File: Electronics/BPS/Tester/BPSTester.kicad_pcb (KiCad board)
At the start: 2 copper layers, 26 parts, among them J1 Conn_01x13_Male

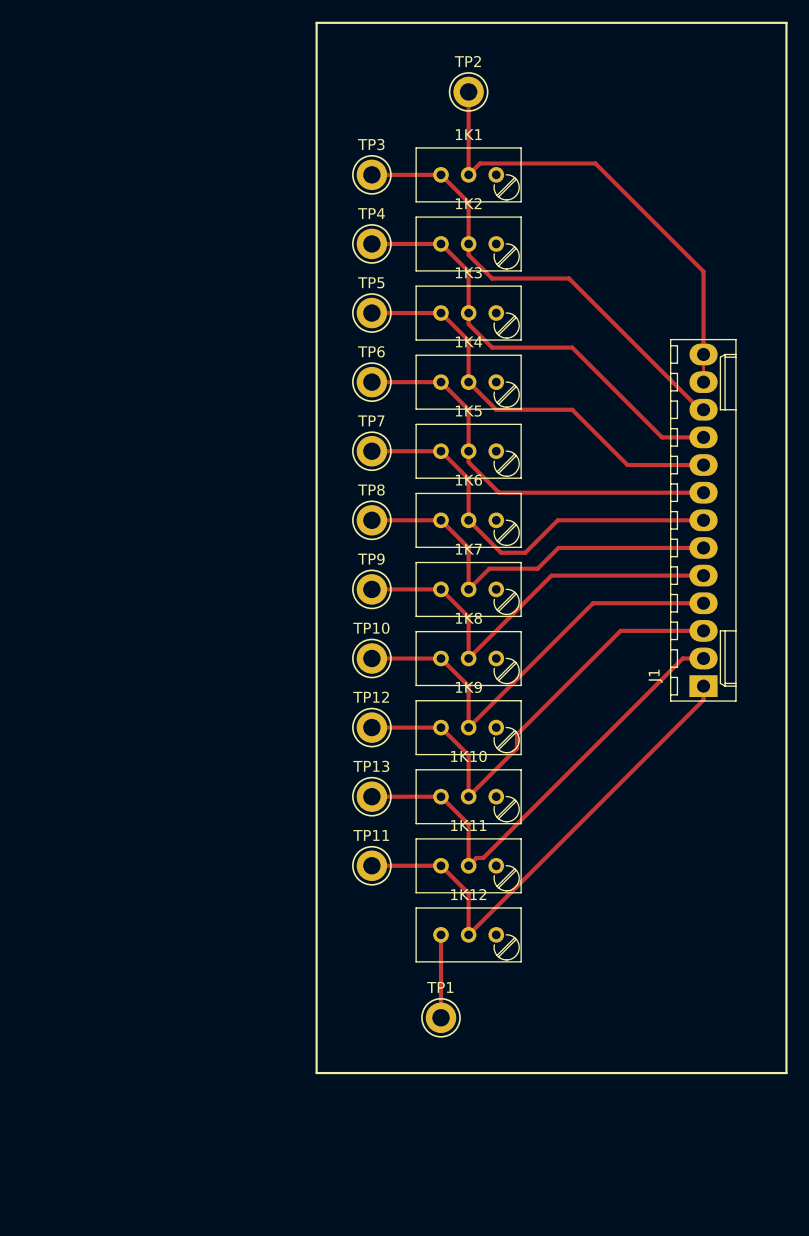
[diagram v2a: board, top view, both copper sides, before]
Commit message: Placed a ground plane and labeled Testing board
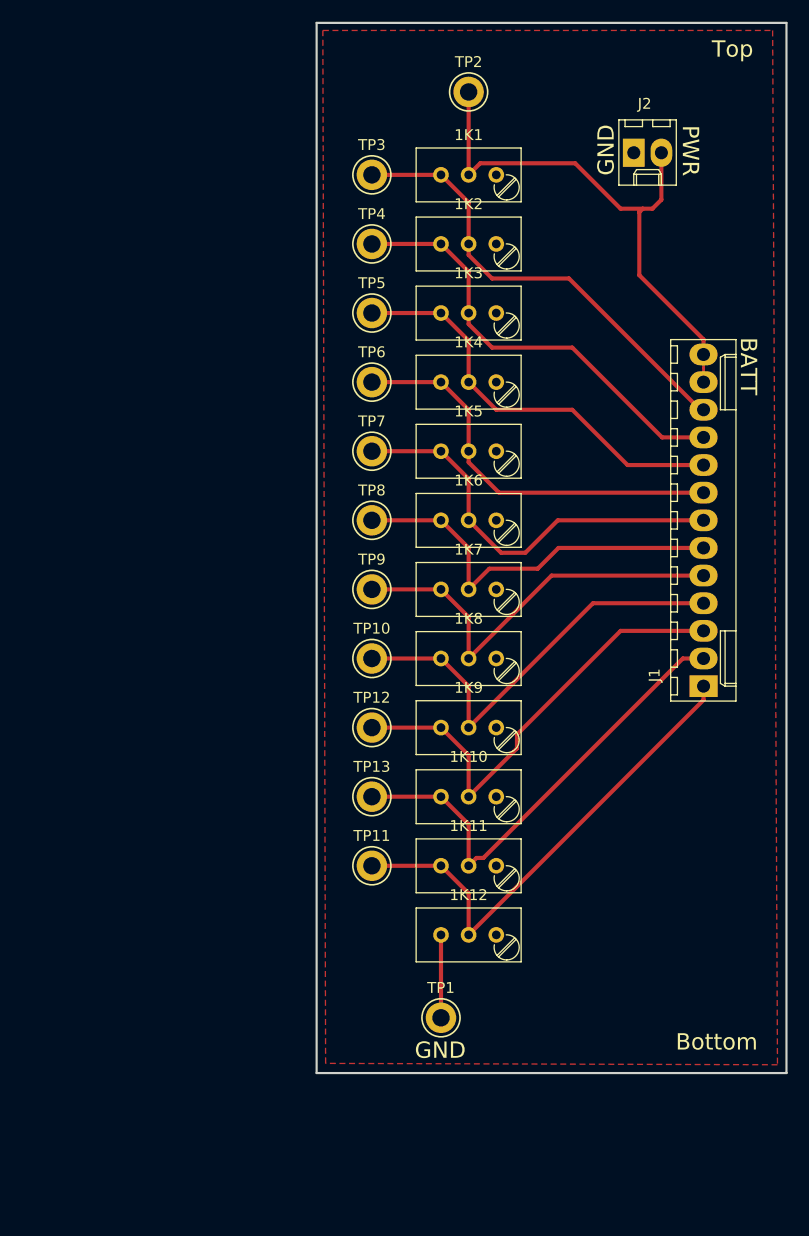
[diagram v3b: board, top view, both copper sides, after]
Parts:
- added J2: Conn_01x02_Male, Connectors_Molex:Molex_KK-6410-02_02x2.54mm_Straight, F.Cu at (156.1, 52.6)
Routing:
- net +BATT: track 43.9 -> 50.7 mm
- net GND: track 7.62 -> 8.19 mm
- added copper zone on F.Cu, net GND
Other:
- board outline added: 43.2 x 96.5 mm
- board text added: "BATT"
- board text added: "Bottom"
- board text added: "GND"
- board text added: "PWR"
- board text added: "Top"
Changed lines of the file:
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@@
   (general
     (thickness 1.6)
-    (drawings 4)
-    (tracks 80)
+    (drawings 10)
+    (tracks 90)
     (zones 0)
-    (modules 26)
+    (modules 27)
     (nets 26)
   )
@@
     (trace_min 0.2)
     (segment_width 0.2)
-    (edge_width 0.15)
+    (edge_width 0.2)
     (via_size 0.762)
     (via_drill 0.381)
@@
     (add_net "Net-(1K8-Pad3)")
     (add_net "Net-(1K9-Pad1)")
+  )
+  (module Connectors_Molex:Molex_KK-6410-02_02x2.54mm_Straight (layer F.Cu)
+    (at 156.1465 52.578)
+    (descr "Connector Headers with Friction Lock, 22-27-2021, http://www.molex.com/pdm_docs/sd/022272021_sd.pdf")
+    (tags "connector molex kk_6410 22-27-2021")
+    (fp_text reference J2 (at 1 -4.5) (layer F.SilkS)
+      (effects (font (size 1 1) (thickness 0.15)))
+    )
+    (fp_text value Conn_01x02_Male (at 1.27 4.5) (layer F.Fab)
+      (effects (font (size 1 1) (thickness 0.15)))
+    )
+    (fp_text user %R (at 1.27 0) (layer F.Fab)
+      (effects (font (size 1 1) (thickness 0.15)))
+    )
+    (fp_line (start 4.45 3.5) (end -1.9 3.5) (layer F.CrtYd) (width 0.05))
+    (fp_line (start 4.45 -3.55) (end 4.45 3.5) (layer F.CrtYd) (width 0.05))
+    (fp_line (start -1.9 -3.55) (end 4.45 -3.55) (layer F.CrtYd) (width 0.05))
+    (fp_line (start -1.9 3.5) (end -1.9 -3.55) (layer F.CrtYd) (width 0.05))
+    (fp_line (start 3.34 -2.4) (end 3.34 -3.02) (layer F.SilkS) (width 0.12))
+    (fp_line (start 1.74 -2.4) (end 3.34 -2.4) (layer F.SilkS) (width 0.12))
+    (fp_line (start 1.74 -3.02) (end 1.74 -2.4) (layer F.SilkS) (width 0.12))
+    (fp_line (start 0.8 -2.4) (end 0.8 -3.02) (layer F.SilkS) (width 0.12))
+    (fp_line (start -0.8 -2.4) (end 0.8 -2.4) (layer F.SilkS) (width 0.12))
+    (fp_line (start -0.8 -3.02) (end -0.8 -2.4) (layer F.SilkS) (width 0.12))
+    (fp_line (start 2.29 2.98) (end 2.29 1.98) (layer F.SilkS) (width 0.12))
+    (fp_line (start 0.25 2.98) (end 0.25 1.98) (layer F.SilkS) (width 0.12))
+    (fp_line (start 2.29 1.55) (end 2.54 1.98) (layer F.SilkS) (width 0.12))
+    (fp_line (start 0.25 1.55) (end 2.29 1.55) (layer F.SilkS) (width 0.12))
+    (fp_line (start 0 1.98) (end 0.25 1.55) (layer F.SilkS) (width 0.12))
+    (fp_line (start 2.54 1.98) (end 2.54 2.98) (layer F.SilkS) (width 0.12))
+    (fp_line (start 0 1.98) (end 2.54 1.98) (layer F.SilkS) (width 0.12))
+    (fp_line (start 0 2.98) (end 0 1.98) (layer F.SilkS) (width 0.12))
+    (fp_line (start 3.91 -3.02) (end -1.37 -3.02) (layer F.SilkS) (width 0.12))
+    (fp_line (start 3.91 2.98) (end 3.91 -3.02) (layer F.SilkS) (width 0.12))
+    (fp_line (start -1.37 2.98) (end 3.91 2.98) (layer F.SilkS) (width 0.12))
+    (fp_line (start -1.37 -3.02) (end -1.37 2.98) (layer F.SilkS) (width 0.12))
+    (fp_line (start 4.01 -3.12) (end -1.47 -3.12) (layer F.Fab) (width 0.12))
+    (fp_line (start 4.01 3.08) (end 4.01 -3.12) (layer F.Fab) (width 0.12))
+    (fp_line (start -1.47 3.08) (end 4.01 3.08) (layer F.Fab) (width 0.12))
+    (fp_line (start -1.47 -3.12) (end -1.47 3.08) (layer F.Fab) (width 0.12))
+    (pad 2 thru_hole oval (at 2.54 0) (size 2 2.6) (drill 1.2) (layers *.Cu *.Mask)
+      (net 2 +BATT))
+    (pad 1 thru_hole rect (at 0 0) (size 2 2.6) (drill 1.2) (layers *.Cu *.Mask)
+      (net 24 GND))
+    (model ${KISYS3DMOD}/Connectors_Molex.3dshapes/Molex_KK-6410-02_02x2.54mm_Straight.wrl
+      (at (xyz 0 0 0))
+      (scale (xyz 1 1 1))
+      (rotate (xyz 0 0 0))
+    )
   )
   (module Potentiometers:Potentiometer_Trimmer_Bourns_3296W (layer F.Cu)
@@
       (net 20 "Net-(1K10-Pad3)"))
   )
-  (gr_line (start 170.18 40.64) (end 127 40.64) (layer F.SilkS) (width 0.2))
-  (gr_line (start 170.18 137.16) (end 170.18 40.64) (layer F.SilkS) (width 0.2))
-  (gr_line (start 127 137.16) (end 170.18 137.16) (layer F.SilkS) (width 0.2))
-  (gr_line (start 127 40.64) (end 127 137.16) (layer F.SilkS) (width 0.2))
-  (segment (start 140.97 46.99) (end 140.97 54.61) (width 0.381) (layer F.Cu) (net 2))
-  (segment (start 142.015001 53.564999) (end 152.624999 53.564999) (width 0.381) (layer F.Cu) (net 2))
-  (segment (start 152.624999 53.564999) (end 162.56 63.5) (width 0.381) (layer F.Cu) (net 2))
-  (segment (start 162.56 63.5) (end 162.56 71.12) (width 0.381) (layer F.Cu) (net 2))
-  (segment (start 140.97 54.61) (end 142.015001 53.564999) (width 0.381) (layer F.Cu) (net 2))
+  (gr_text "BATT\n" (at 166.6875 72.1995 270) (layer F.SilkS)
+    (effects (font (size 1.5 1.5) (thickness 0.3)))
+  )
+  (gr_text GND (at 138.3665 135.0645) (layer F.SilkS)
+    (effects (font (size 1.5 1.5) (thickness 0.3)))
+  )
+  (gr_text PWR (at 161.3535 52.3875 270) (layer F.SilkS)
+    (effects (font (size 1.5 1.5) (thickness 0.3)))
+  )
+  (gr_text "GND\n" (at 153.6065 52.324 90) (layer F.SilkS)
+    (effects (font (size 1.5 1.5) (thickness 0.3)))
+  )
+  (gr_text Top (at 165.227 43.053) (layer F.SilkS)
+    (effects (font (size 1.5 1.5) (thickness 0.3)))
+  )
+  (gr_text "Bottom\n" (at 163.7665 134.3025) (layer F.SilkS)
+    (effects (font (size 1.5 1.5) (thickness 0.3)))
+  )
+  (gr_line (start 170.18 40.64) (end 127 40.64) (layer Edge.Cuts) (width 0.2))
+  (gr_line (start 170.18 137.16) (end 170.18 40.64) (layer Edge.Cuts) (width 0.2))
+  (gr_line (start 127 137.16) (end 170.18 137.16) (layer Edge.Cuts) (width 0.2))
+  (gr_line (start 127 40.64) (end 127 137.16) (layer Edge.Cuts) (width 0.2))
   (segment (start 162.56 72.37) (end 162.56 73.66) (width 0.25) (layer F.Cu) (net 2))
   (segment (start 162.56 71.12) (end 162.56 72.37) (width 0.25) (layer F.Cu) (net 2))
+  (segment (start 140.97 46.99) (end 140.97 54.61) (width 0.381) (layer F.Cu) (net 2))
+  (segment (start 142.032901 53.547099) (end 150.765599 53.547099) (width 0.381) (layer F.Cu) (net 2))
+  (segment (start 140.97 54.61) (end 142.032901 53.547099) (width 0.381) (layer F.Cu) (net 2))
+  (segment (start 150.765599 53.547099) (end 154.94 57.7215) (width 0.381) (layer F.Cu) (net 2))
+  (segment (start 158.6865 56.896) (end 158.6865 52.578) (width 0.381) (layer F.Cu) (net 2))
+  (segment (start 157.861 57.7215) (end 158.6865 56.896) (width 0.381) (layer F.Cu) (net 2))
+  (segment (start 162.56 69.739) (end 156.6545 63.8335) (width 0.381) (layer F.Cu) (net 2))
+  (segment (start 162.56 71.12) (end 162.56 69.739) (width 0.381) (layer F.Cu) (net 2))
+  (segment (start 156.6545 58.039) (end 156.972 57.7215) (width 0.381) (layer F.Cu) (net 2))
+  (segment (start 156.6545 63.8335) (end 156.6545 58.039) (width 0.381) (layer F.Cu) (net 2))
+  (segment (start 154.94 57.7215) (end 156.972 57.7215) (width 0.381) (layer F.Cu) (net 2))
+  (segment (start 156.972 57.7215) (end 157.861 57.7215) (width 0.381) (layer F.Cu) (net 2))
   (segment (start 132.08 54.61) (end 138.43 54.61) (width 0.381) (layer F.Cu) (net 3))
   (segment (start 140.97 57.15) (end 140.97 60.96) (width 0.381) (layer F.Cu) (net 3))
@@
   (segment (start 162.56 102.87) (end 162.56 101.6) (width 0.381) (layer F.Cu) (net 23))
   (segment (start 140.97 124.46) (end 162.56 102.87) (width 0.381) (layer F.Cu) (net 23))
+  (segment (start 156.1465 52.278) (end 156.2735 52.151) (width 0.381) (layer F.Cu) (net 24))
+  (segment (start 156.1465 52.578) (end 156.1465 52.278) (width 0.381) (layer F.Cu) (net 24))
+  (segment (start 156.1465 52.278) (end 156.083 52.2145) (width 0.381) (layer F.Cu) (net 24))
   (segment (start 138.43 124.46) (end 138.43 132.08) (width 0.381) (layer F.Cu) (net 24))
+  (zone (net 24) (net_name GND) (layer F.Cu) (hatch edge 0.508)
+    (connect_pads (clearance 0.508))
+    (min_thickness 0.254)
+    (fill yes (arc_segments 16) (thermal_gap 0.508) (thermal_bridge_width 0.508))
+    (polygon
+      (pts
+        (xy 127.5715 41.3385) (xy 168.91 41.3385) (xy 169.3545 136.398) (xy 127.8255 136.271)
+      )
+    )
+  )
 )

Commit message: Finalized all boards. Created gerber files.
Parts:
- added G***: LOGO, UTSVT_Special:UTSVT_Logo_Symbol, F.Cu at (136.0, 137.0)
- added REF**: MountingHole_3mm, MountingHole:MountingHole_3mm, F.Cu at (103.0, 147.0)
- added REF**: MountingHole_3mm, MountingHole:MountingHole_3mm, F.Cu at (147.0, 147.0)
- added REF**: MountingHole_3mm, MountingHole:MountingHole_3mm, F.Cu at (147.0, 53.0)
- added REF**: MountingHole_3mm, MountingHole:MountingHole_3mm, F.Cu at (103.0, 53.0)
- moved TP11 25.8 mm to (108.8, 129.4)
- moved TP10 25.8 mm to (108.8, 110.3)
- moved TP12 25.8 mm to (108.8, 116.7)
- moved TP13 25.8 mm to (108.8, 123.0)
- moved TP3 25.8 mm to (108.8, 65.9)
- moved TP4 25.8 mm to (108.8, 72.2)
- moved TP5 25.8 mm to (108.8, 78.6)
- moved TP6 25.8 mm to (108.8, 84.9)
- moved TP7 25.8 mm to (108.8, 91.3)
- moved TP8 25.8 mm to (108.8, 97.6)
- moved TP9 25.8 mm to (108.8, 104.0)
- moved J1 25.8 mm to (139.3, 112.8)
- moved J2 25.8 mm to (132.9, 63.8)
- moved TP1 25.8 mm to (115.2, 143.3)
- moved TP2 25.8 mm to (117.7, 58.2)
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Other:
- board size 43.2 x 96.5 mm -> 50 x 100 mm
- board text added: "Spring 2019: Monolo Alvarez Chase Block Corbin Capo Richard Li Austin Tsao Garrett Wong Sihyung Woo Sijin Woo"
- board text added: "UTSVT - BPS Volt. Test v1.0 Spring 2019 Garrett Wong"
